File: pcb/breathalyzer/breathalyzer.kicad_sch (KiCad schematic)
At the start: 26 parts, among them IC1 TPS3840DL25DBVR, J1 Conn_01x07_Pin, SW1 PTS636SK43SMTR, SW2 430162085826, U1 STM32F030K6Tx, U2 TLV73325PDBV, U4 TLV61070ADBV, U5 AY0438X-L

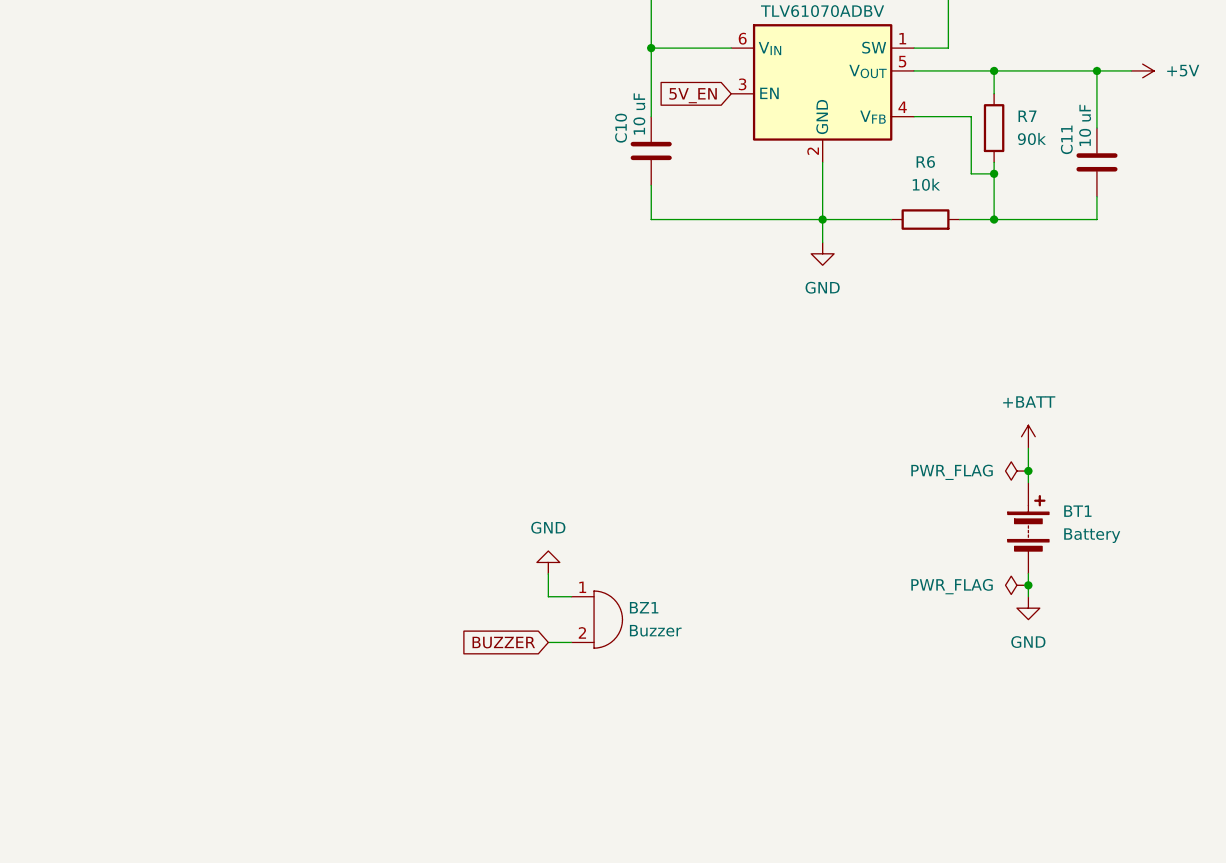
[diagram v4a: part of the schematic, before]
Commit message: reverse polarity protection
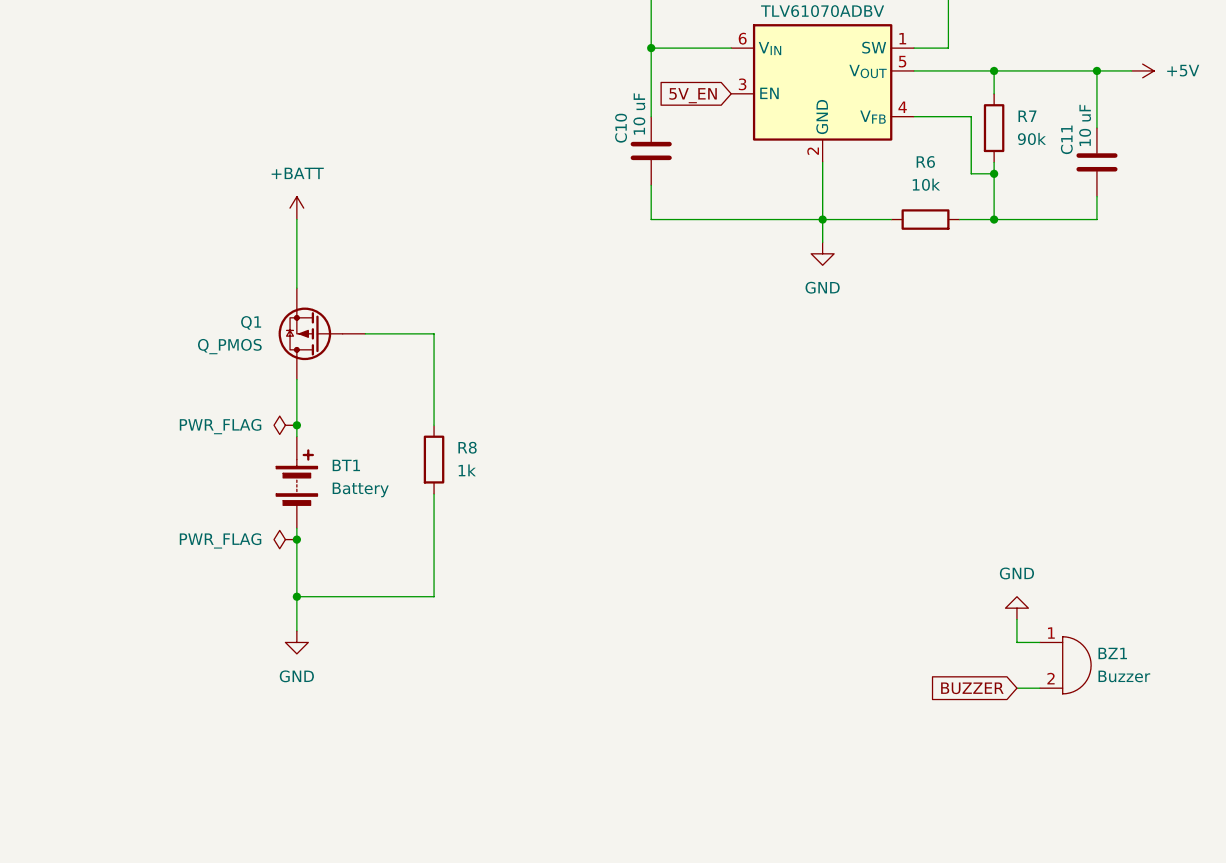
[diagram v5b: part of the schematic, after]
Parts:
- added Q1: Q_PMOS, Package_TO_SOT_SMD:SOT-23-3, symbol Device:Q_PMOS
- added R8: 1k, Resistor_SMD:R_0603_1608Metric, symbol Device:R
- BT1: footprint (none) -> breathalyzer:SHDRRA2W50P0X200_1X2_600X770X525P
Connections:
- net +BATT: now also Q1.2 (S); no longer BT1.1 (+)
- net GND: now also R8.2
- new net: Q1.1 (G), R8.1
- new net: BT1.1 (+), Q1.3 (D)
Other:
- moved on the sheet: BT1, BZ1

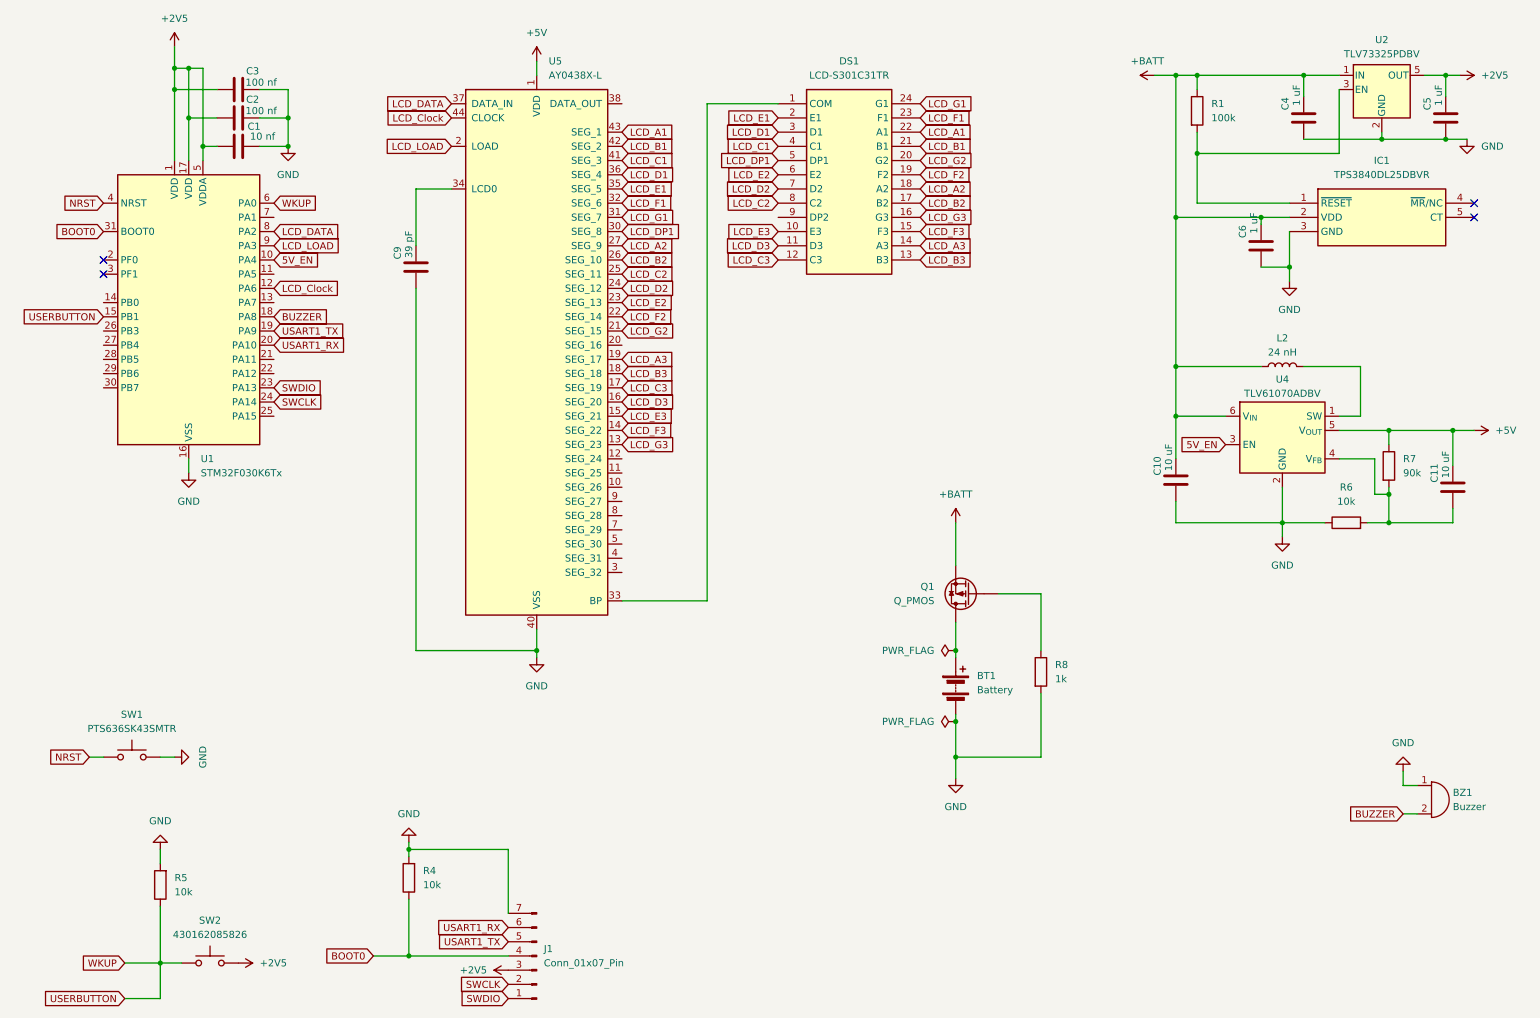
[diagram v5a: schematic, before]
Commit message: changed power supply
5V boost from BATT
2V5 LDO from 5V
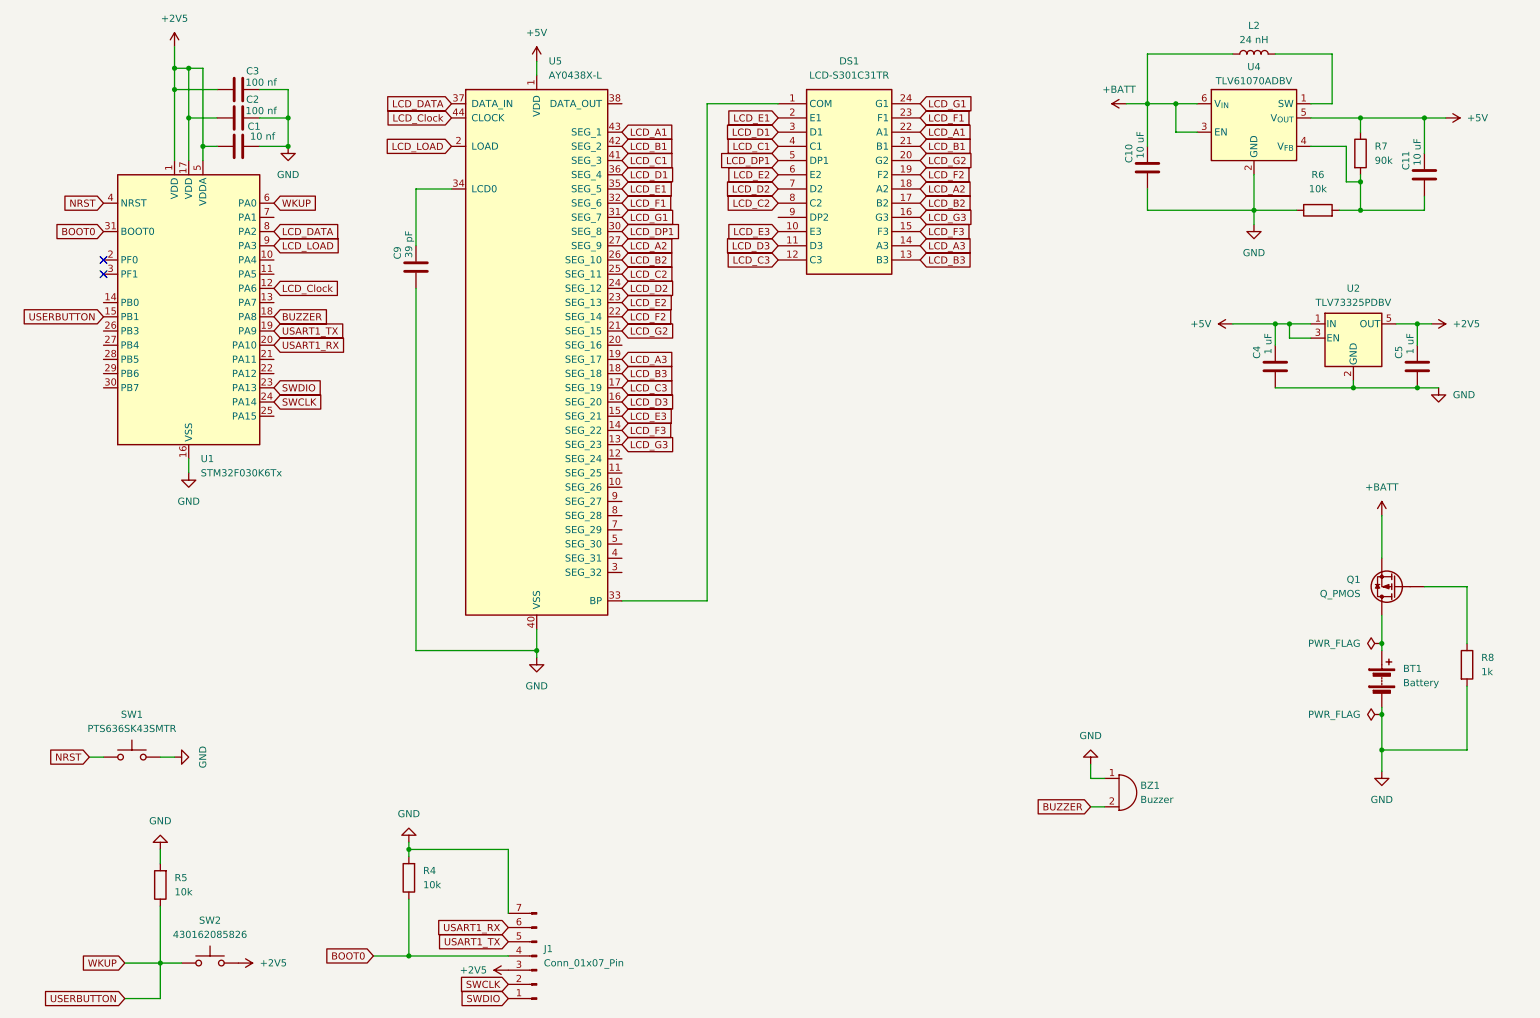
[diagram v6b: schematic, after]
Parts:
- removed C6: 1 uF, Capacitor_SMD:C_0603_1608Metric, symbol Device:C
- removed IC1: TPS3840DL25DBVR, Package_TO_SOT_SMD:SOT-23-5_HandSoldering, symbol breathalyzer:TPS3840DL25DBVR
- removed R1: 100k, Resistor_SMD:R_0402_1005Metric, symbol Device:R
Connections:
- net +2V5: now also SW2.3; no longer SW2.2
- net +5V: now also C4.2, U2.1 (IN), U2.3 (EN)
- net +BATT: now also U4.3 (EN); no longer C4.2, U2.1 (IN)
- net 5V_EN: no longer names the net of U1.10 (PA4)
- net 5V_EN: no longer U4.3 (EN)
- no-connect marks 4 -> 2
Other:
- moved on the sheet: BT1, BZ1, C10, C11, C4, C5, L2, Q1, R6, R7, R8, U2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

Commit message: sensor connector
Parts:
- added J2: MP-3B socket, breathalyzer:25SHB04TS, symbol Connector:Conn_01x04_Socket
- added Q2: NPN, Package_TO_SOT_SMD:SOT-23-3, symbol Simulation_SPICE:NPN
- added R1: 50k_Variable, Potentiometer_THT:Potentiometer_ACP_CA9-H5_Horizontal, symbol Device:R_Variable
- added R2: 330, Resistor_SMD:R_0805_2012Metric, symbol Device:R
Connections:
- net +2V5: now also J2.1 (Pin_1), J2.3 (Pin_3)
- net GND: now also Q2.3 (E), R1.2
- net SENSOR_EN: now reaches U1.10 (PA4)
- net SENSOR_EN: now also R2.2
- net ADC_IN: now reaches U1.7 (PA1)
- net ADC_IN: now also J2.4 (Pin_4), R1.1
- new net: J2.2 (Pin_2), Q2.1 (C)
- new net: Q2.2 (B), R2.1
